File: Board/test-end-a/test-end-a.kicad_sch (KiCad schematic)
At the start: 37 parts, among them J10 SW2, J11 TENDA_2, J12 TENDA_1, J2 I2C connector, J5 VAC 230V, J6 VDC 5V, J7 SW1, J8 Anemometer, J9 TX RX - + Serial TTL, K1 FINDER-36.11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

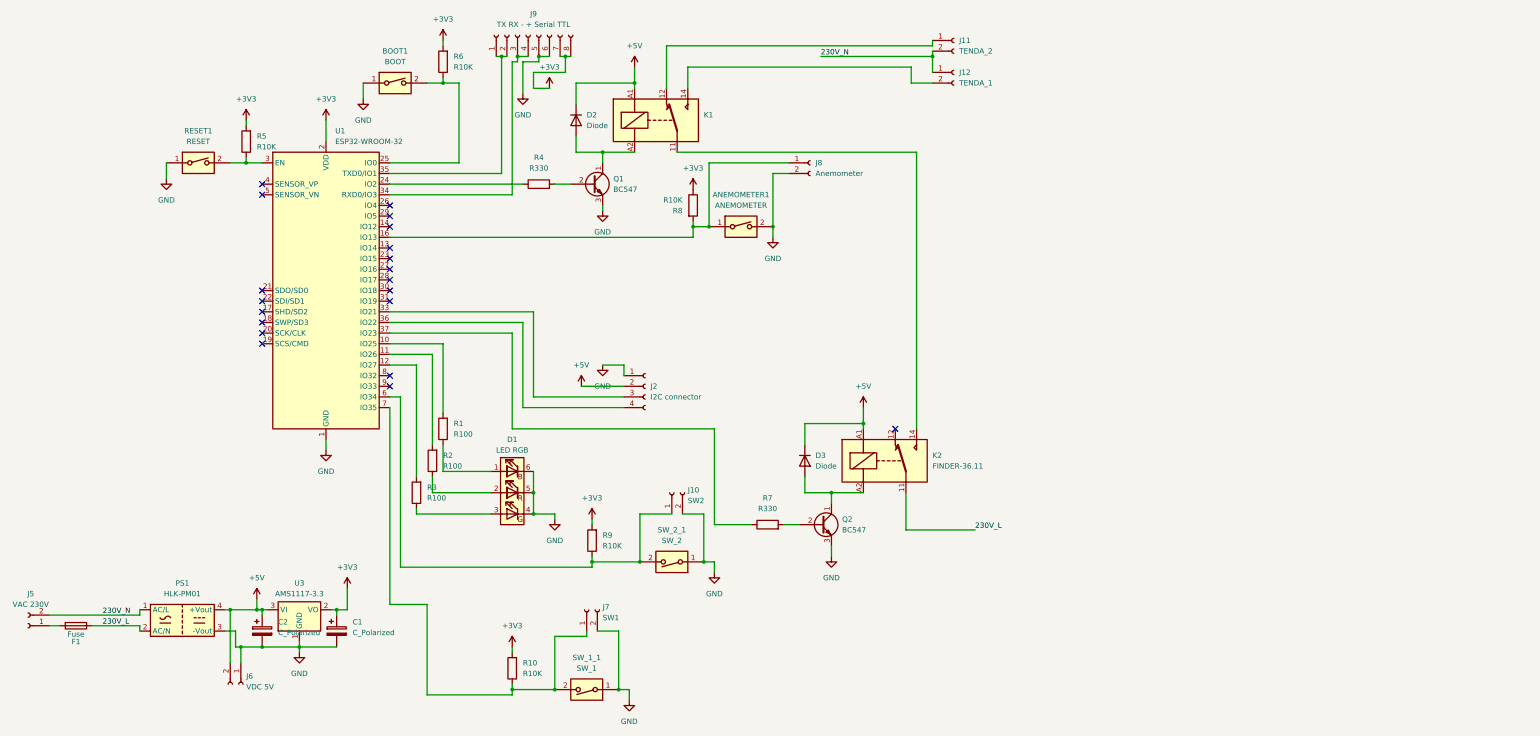
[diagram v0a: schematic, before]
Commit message: [ADD] Add consumption scheme and components on the board
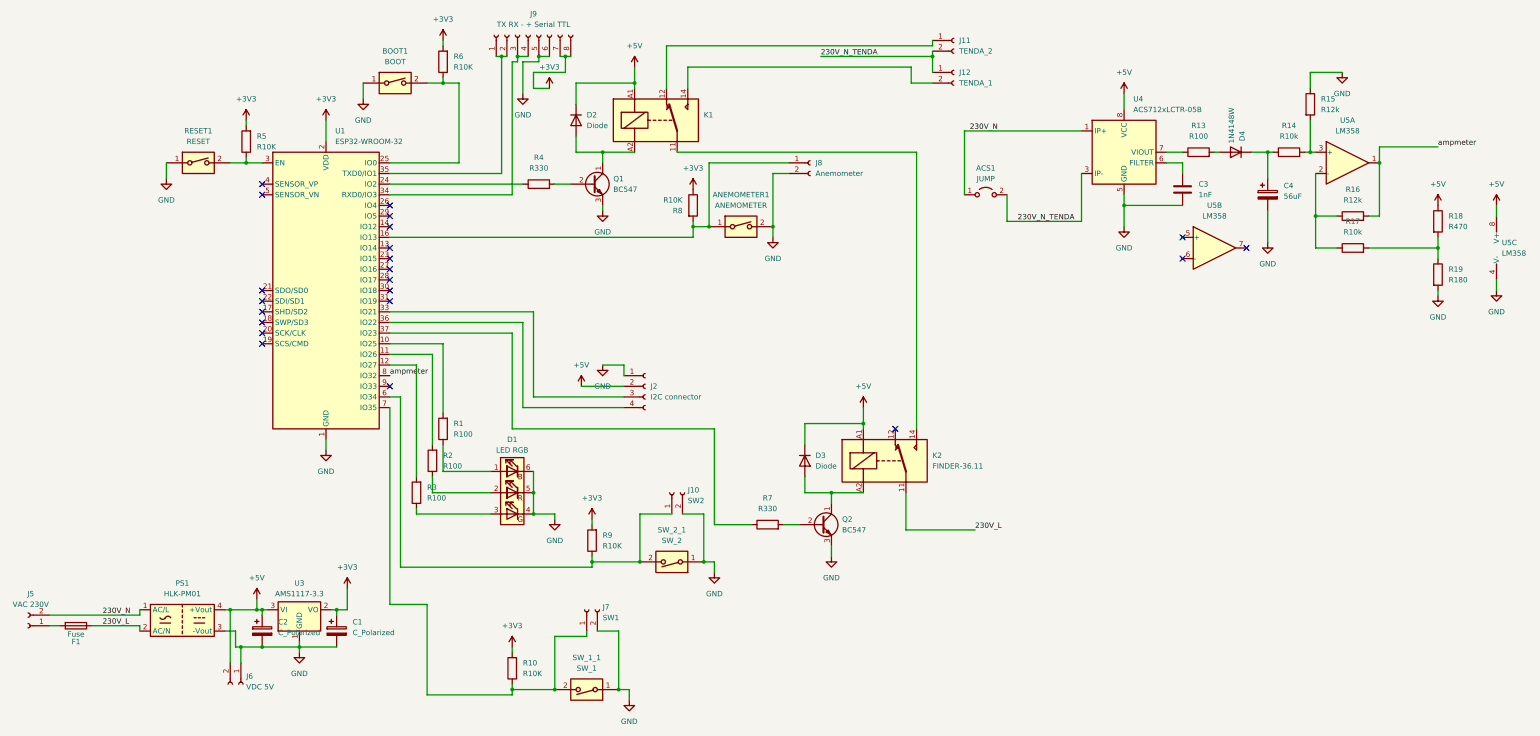
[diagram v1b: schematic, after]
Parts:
- added ACS1: JUMP, Jumper:SolderJumper-2_P1.3mm_Open_RoundedPad1.0x1.5mm, symbol Jumper:Jumper_2_Open
- added C3: 1nF, Inductor_SMD:L_1206_3216Metric_Pad1.22x1.90mm_HandSolder, symbol Device:C
- added C4: 56uF, Capacitor_THT:CP_Radial_D10.0mm_P5.00mm, symbol Device:C_Polarized
- added D4: 1N4148W, Diode_SMD:D_SOD-123, symbol Diode:1N4148W
- added R13: R100, Resistor_SMD:R_1206_3216Metric, symbol Device:R
- added R14, R17: R10k, Resistor_SMD:R_1206_3216Metric, symbol Device:R
- added R15, R16: R12k, Resistor_SMD:R_1206_3216Metric, symbol Device:R
- added R18: R470, Resistor_SMD:R_1206_3216Metric, symbol Device:R
- added R19: R180, Resistor_SMD:R_1206_3216Metric, symbol Device:R
- added U4: ACS712xLCTR-05B, Package_SO:SOIC-8_3.9x4.9mm_P1.27mm, symbol Sensor_Current:ACS712xLCTR-05B
- added U5: LM358, Package_SO:SOIC-8-1EP_3.9x4.9mm_P1.27mm_EP2.29x3mm, symbol Amplifier_Operational:LM358
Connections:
- net +5V: now also R18.1, U4.8 (VCC), U5.8 (V+)
- net 230V_N: now also ACS1.1 (A), U4.1 (IP+), U4.2 (IP+); no longer J11.2 (Pin_2), J12.1 (Pin_1)
- net GND: now also C3.2, C4.2, R15.1, R19.2, U4.5 (GND), U5.4 (V-)
- net ampmeter: now reaches U1.8 (IO32)
- net ampmeter: now also R16.2, U5.1
- new net: R16.1, R17.1, U5.2 (-)
- new net: R14.2, R15.2, U5.3 (+)
- new net: R17.2, R18.2, R19.1
- new net: C3.1, U4.6 (FILTER)
- new net: R13.1, U4.7 (VIOUT)
- new net: C4.1, D4.1 (K), R14.1
- new net: D4.2 (A), R13.2
- new net 230V_N_TENDA: ACS1.2 (B), J11.2 (Pin_2), J12.1 (Pin_1), U4.3 (IP-), U4.4 (IP-)
- no-connect marks 20 -> 22

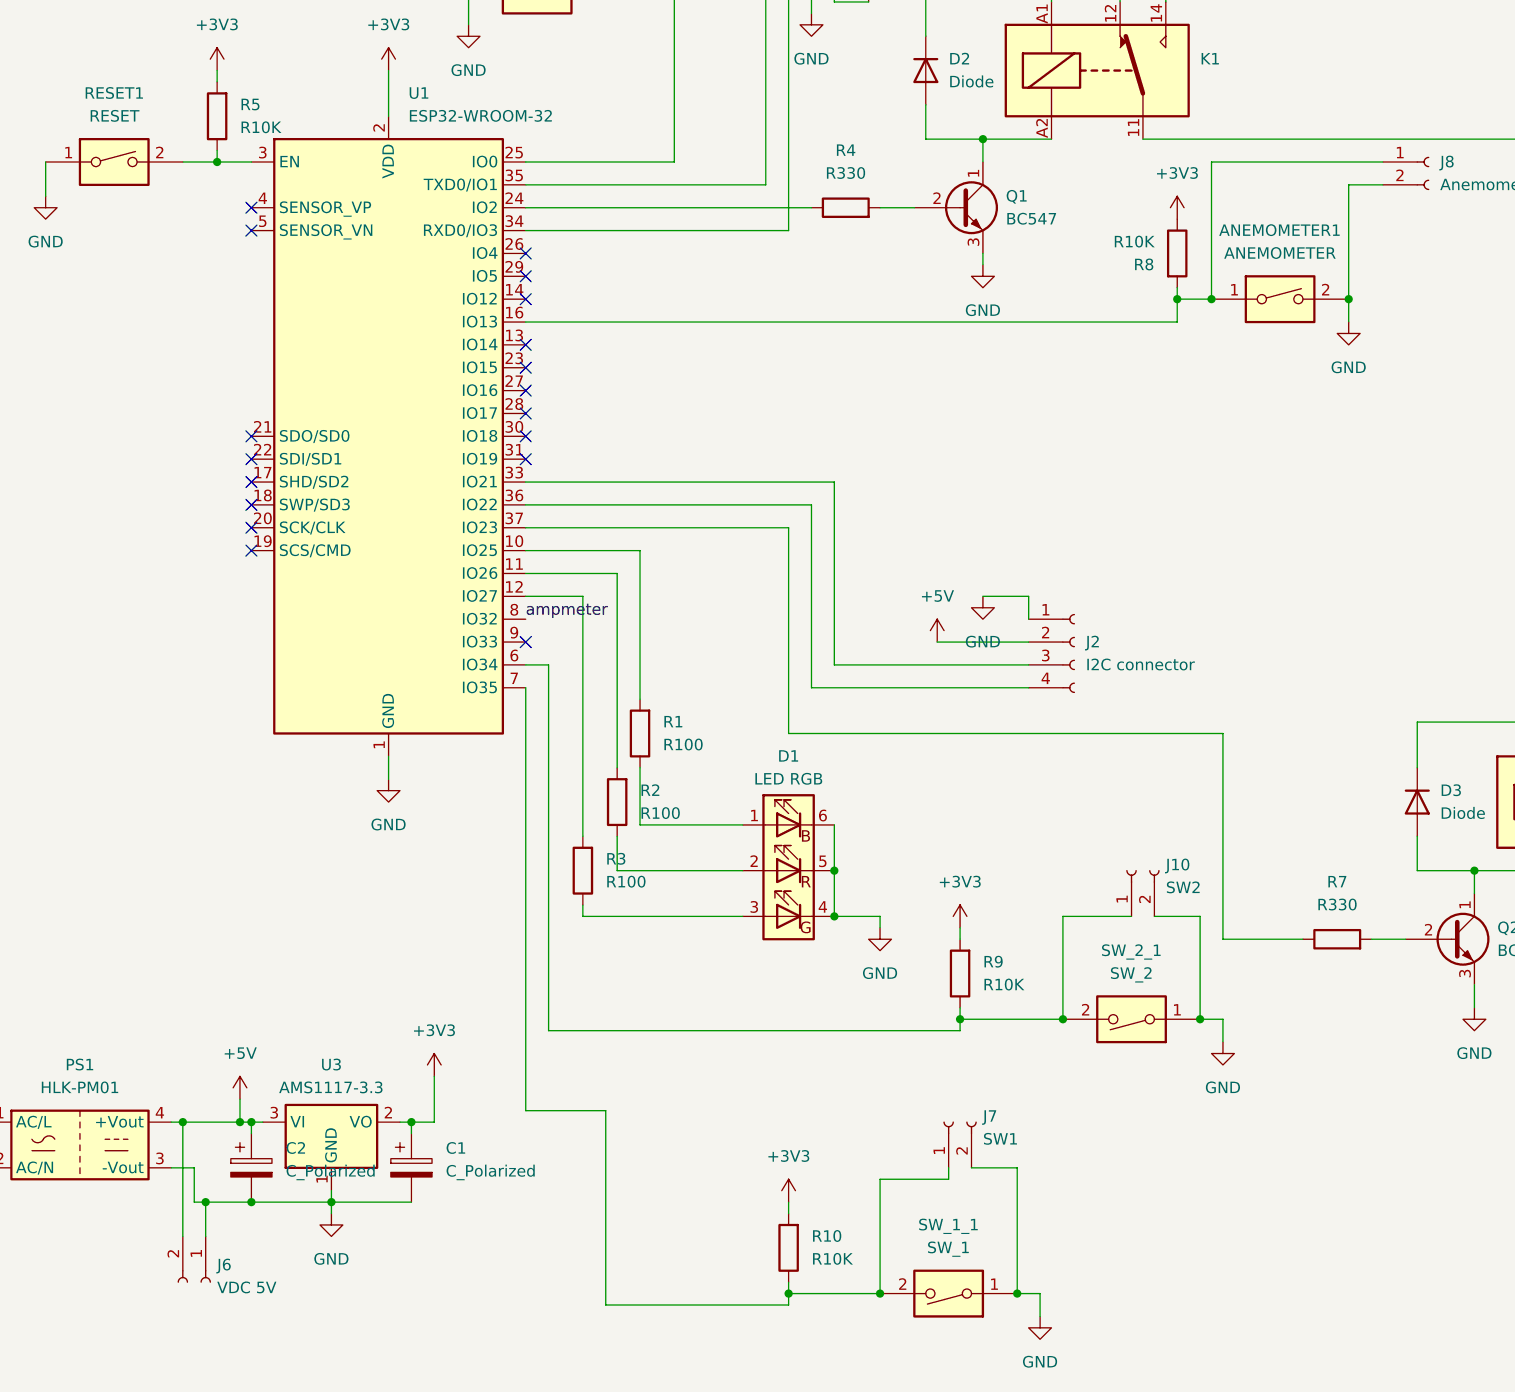
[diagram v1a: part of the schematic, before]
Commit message: [FIX] Fix board dimensions
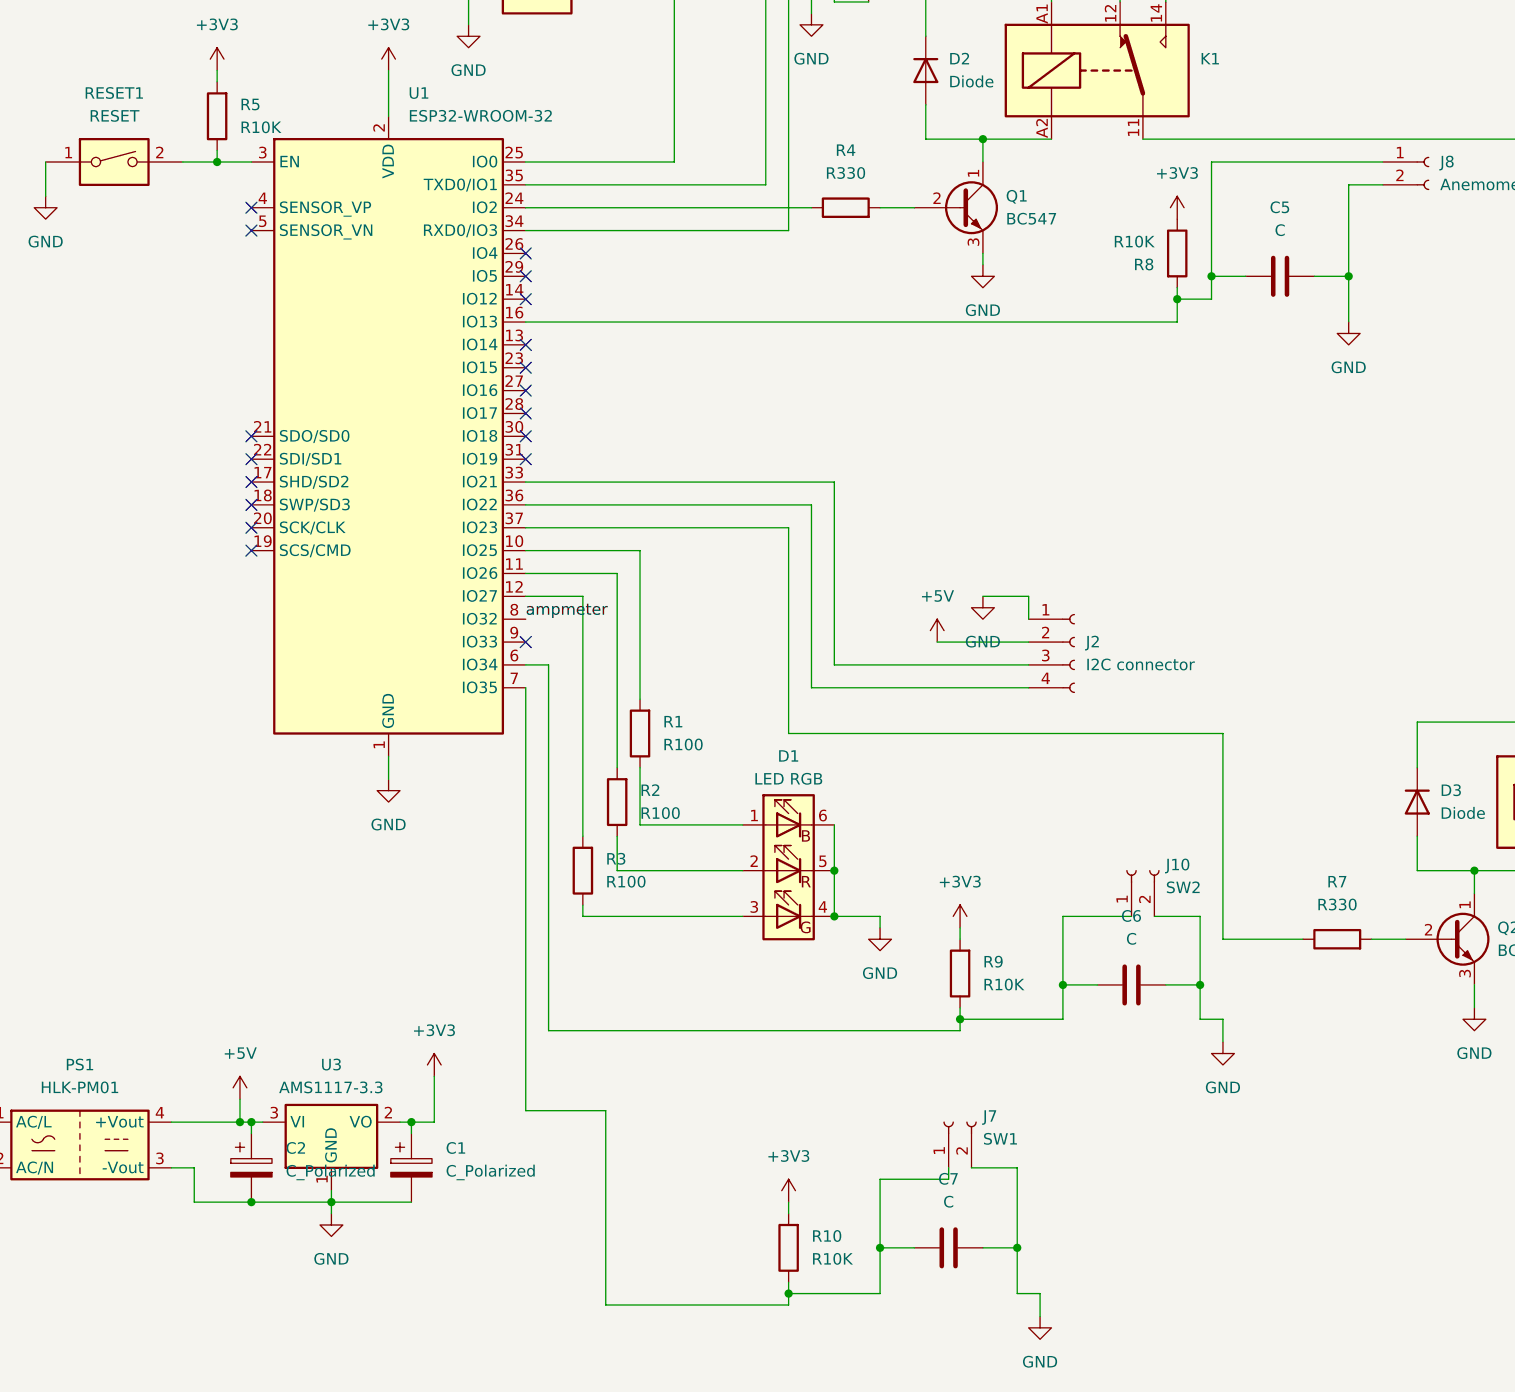
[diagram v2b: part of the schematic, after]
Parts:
- removed ANEMOMETER1: ANEMOMETER, Button_Switch_THT:SW_PUSH_6mm_H4.3mm, symbol Switch:SW_DIP_x01
- removed J6: VDC 5V, TerminalBlock:TerminalBlock_Altech_AK300-2_P5.00mm, symbol Connector:Conn_01x02_Socket
- removed SW_1_1: SW_1, Button_Switch_THT:SW_PUSH_6mm_H4.3mm, symbol Switch:SW_DIP_x01
- removed SW_2_1: SW_2, Button_Switch_THT:SW_PUSH_6mm_H4.3mm, symbol Switch:SW_DIP_x01
- added C5, C6, C7: C, Capacitor_THT:C_Disc_D8.0mm_W2.5mm_P5.00mm, symbol Device:C
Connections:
- net GND: now also C5.2, C6.2, C7.2
- net at J8.1 (Pin_1), R8.2, U1.16 (IO13): now also C5.1
- net at J10.1 (Pin_1), R9.1, U1.6 (IO34): now also C6.1
- net at J7.1 (Pin_1), R10.1, U1.7 (IO35): now also C7.1
